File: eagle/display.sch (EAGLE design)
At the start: 6 parts

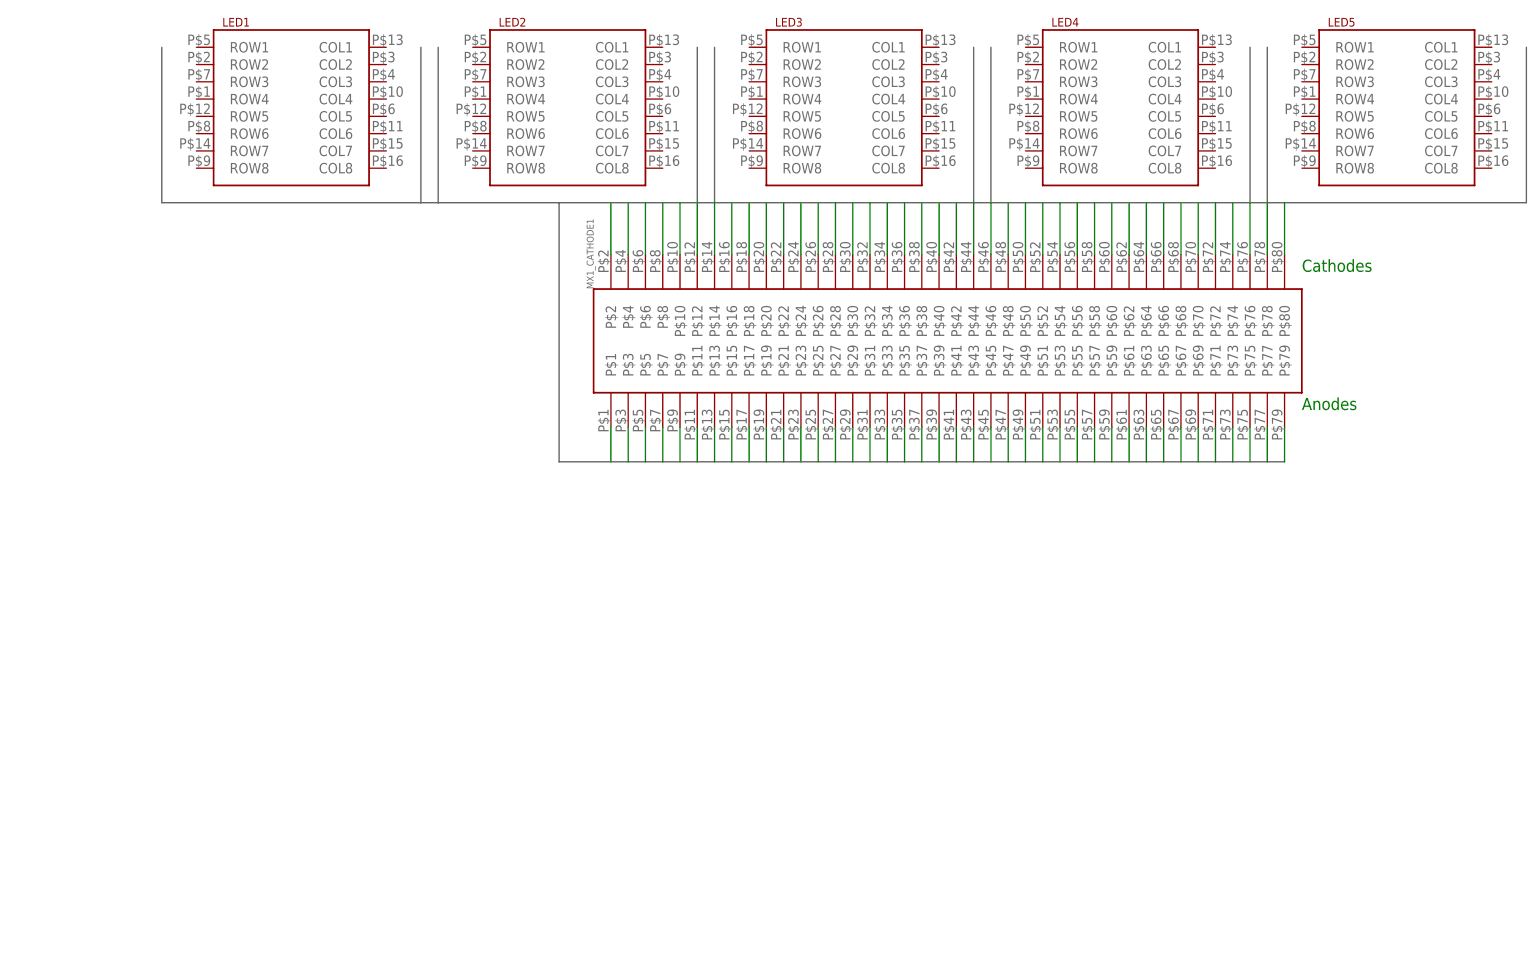
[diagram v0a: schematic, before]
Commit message: removed pinhead
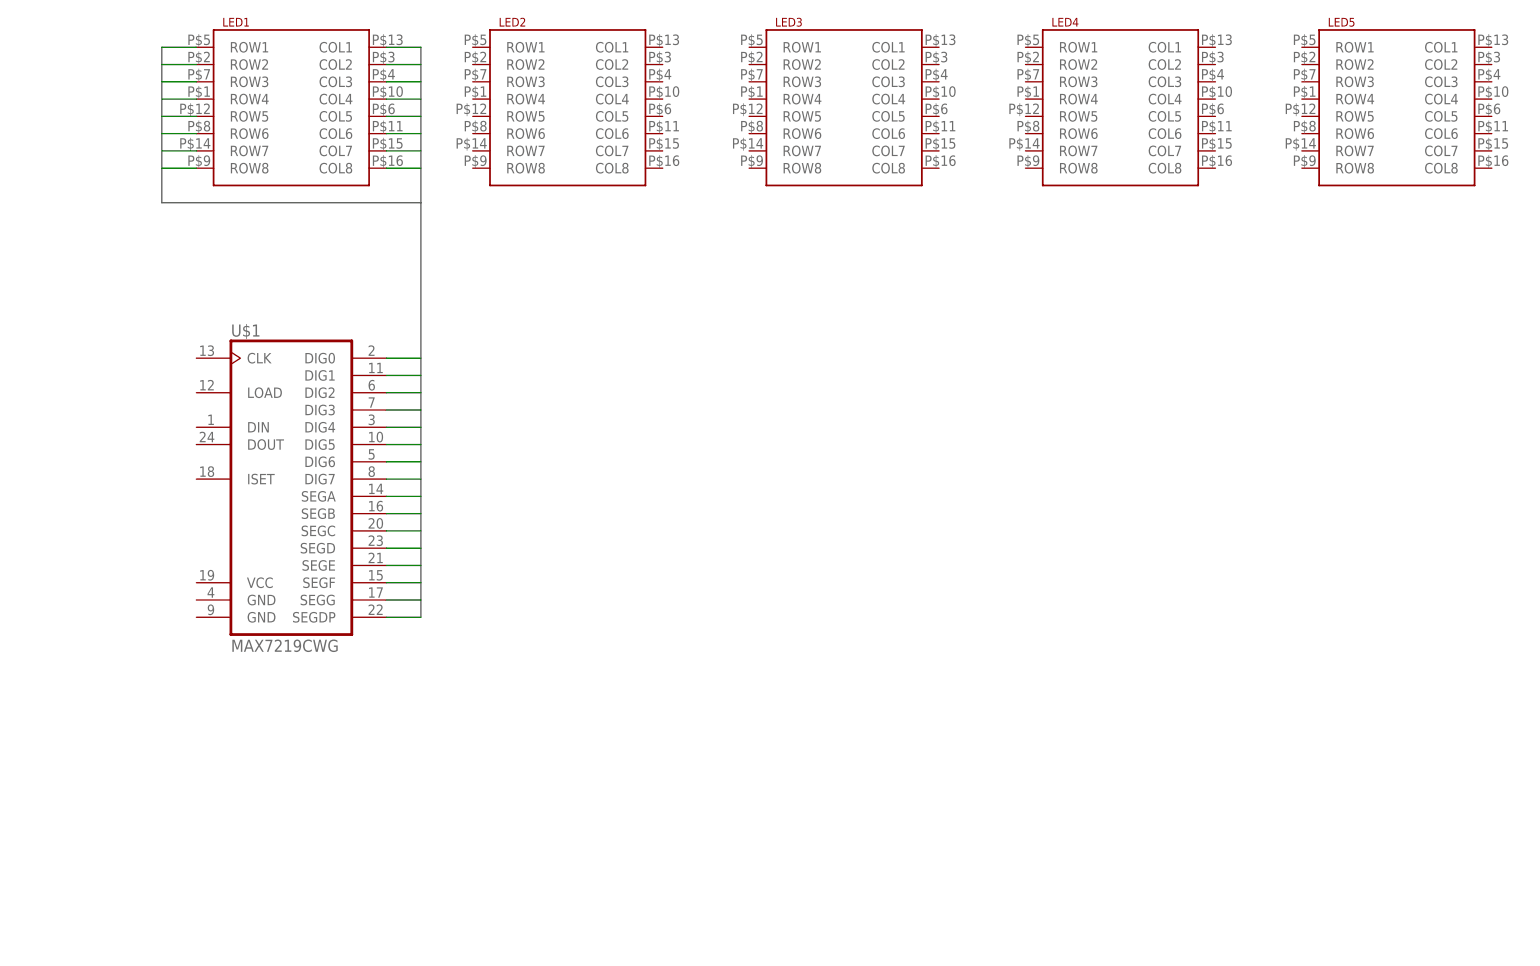
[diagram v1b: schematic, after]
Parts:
- removed U$6: PINHD-2X40FEMALE, pinhead-1.27:PINHD-2X40FEMALE
- added U$1: MAX7219CWG, max7219:MAX7219CWG
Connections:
- removed net MX1_ANODE1: U$6.P$1
- removed net MX1_ANODE2: U$6.P$3
- removed net MX1_ANODE3: U$6.P$5
- removed net MX1_ANODE4: U$6.P$7
- removed net MX1_ANODE5: U$6.P$9
- removed net MX1_ANODE6: U$6.P$11
- removed net MX1_ANODE7: U$6.P$13
- removed net MX1_ANODE8: U$6.P$15
- removed net MX1_CATHODE1: U$6.P$2
- removed net MX1_CATHODE2: U$6.P$4
- removed net MX1_CATHODE3: U$6.P$6
- removed net MX1_CATHODE4: U$6.P$8
- removed net MX1_CATHODE5: U$6.P$10
- removed net MX1_CATHODE6: U$6.P$12
- removed net MX1_CATHODE7: U$6.P$14
- removed net MX1_CATHODE8: U$6.P$16
- removed net MX2_ANODE1: U$6.P$17
- removed net MX2_ANODE2: U$6.P$19
- removed net MX2_ANODE3: U$6.P$21
- removed net MX2_ANODE4: U$6.P$23
- removed net MX2_ANODE5: U$6.P$25
- removed net MX2_ANODE6: U$6.P$27
- removed net MX2_ANODE7: U$6.P$29
- removed net MX2_ANODE8: U$6.P$31
- removed net MX2_CATHODE1: U$6.P$18
- removed net MX2_CATHODE2: U$6.P$20
- removed net MX2_CATHODE3: U$6.P$22
- removed net MX2_CATHODE4: U$6.P$24
- removed net MX2_CATHODE5: U$6.P$26
- removed net MX2_CATHODE6: U$6.P$28
- removed net MX2_CATHODE7: U$6.P$30
- removed net MX2_CATHODE8: U$6.P$32
- removed net MX3_ANODE1: U$6.P$33
- removed net MX3_ANODE2: U$6.P$35
- removed net MX3_ANODE3: U$6.P$37
- removed net MX3_ANODE4: U$6.P$39
- removed net MX3_ANODE5: U$6.P$41
- removed net MX3_ANODE6: U$6.P$43
- removed net MX3_ANODE7: U$6.P$45
- removed net MX3_ANODE8: U$6.P$47
- removed net MX3_CATHODE1: U$6.P$34
- removed net MX3_CATHODE2: U$6.P$36
- removed net MX3_CATHODE3: U$6.P$38
- removed net MX3_CATHODE4: U$6.P$40
- removed net MX3_CATHODE5: U$6.P$42
- removed net MX3_CATHODE6: U$6.P$44
- removed net MX3_CATHODE7: U$6.P$46
- removed net MX3_CATHODE8: U$6.P$48
- removed net MX4_ANODE1: U$6.P$49
- removed net MX4_ANODE2: U$6.P$51
- removed net MX4_ANODE3: U$6.P$53
- removed net MX4_ANODE4: U$6.P$55
- removed net MX4_ANODE5: U$6.P$57
- removed net MX4_ANODE6: U$6.P$59
- removed net MX4_ANODE7: U$6.P$61
- removed net MX4_ANODE8: U$6.P$63
- removed net MX4_CATHODE1: U$6.P$50
- removed net MX4_CATHODE2: U$6.P$52
- removed net MX4_CATHODE3: U$6.P$54
- removed net MX4_CATHODE4: U$6.P$56
- removed net MX4_CATHODE5: U$6.P$58
- removed net MX4_CATHODE6: U$6.P$60
- removed net MX4_CATHODE7: U$6.P$62
- removed net MX4_CATHODE8: U$6.P$64
- removed net MX5_ANODE1: U$6.P$65
- removed net MX5_ANODE2: U$6.P$67
- removed net MX5_ANODE3: U$6.P$69
- removed net MX5_ANODE4: U$6.P$71
- removed net MX5_ANODE5: U$6.P$73
- removed net MX5_ANODE6: U$6.P$75
- removed net MX5_ANODE7: U$6.P$77
- removed net MX5_ANODE8: U$6.P$79
- removed net MX5_CATHODE1: U$6.P$66
- removed net MX5_CATHODE2: U$6.P$68
- removed net MX5_CATHODE3: U$6.P$70
- removed net MX5_CATHODE4: U$6.P$72
- removed net MX5_CATHODE5: U$6.P$74
- removed net MX5_CATHODE6: U$6.P$76
- removed net MX5_CATHODE7: U$6.P$78
- removed net MX5_CATHODE8: U$6.P$80
- new net ANODE1: LED1.ROW1, U$1.SEGA
- new net ANODE2: LED1.ROW2, U$1.SEGB
- new net ANODE3: LED1.ROW3, U$1.SEGC
- new net ANODE4: LED1.ROW4, U$1.SEGD
- new net ANODE5: LED1.ROW5, U$1.SEGE
- new net ANODE6: LED1.ROW6, U$1.SEGF
- new net ANODE7: LED1.ROW7, U$1.SEGG
- new net ANODE8: LED1.ROW8, U$1.SEGDP
- new net CATHODE1: LED1.COL1, U$1.DIG0
- new net CATHODE2: LED1.COL2, U$1.DIG1
- new net CATHODE3: LED1.COL3, U$1.DIG2
- new net CATHODE4: LED1.COL4, U$1.DIG3
- new net CATHODE5: LED1.COL5, U$1.DIG4
- new net CATHODE6: LED1.COL6, U$1.DIG5
- new net CATHODE7: LED1.COL7, U$1.DIG6
- new net CATHODE8: LED1.COL8, U$1.DIG7
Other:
- note removed: "Anodes"
- note removed: "Cathodes"

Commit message: display board
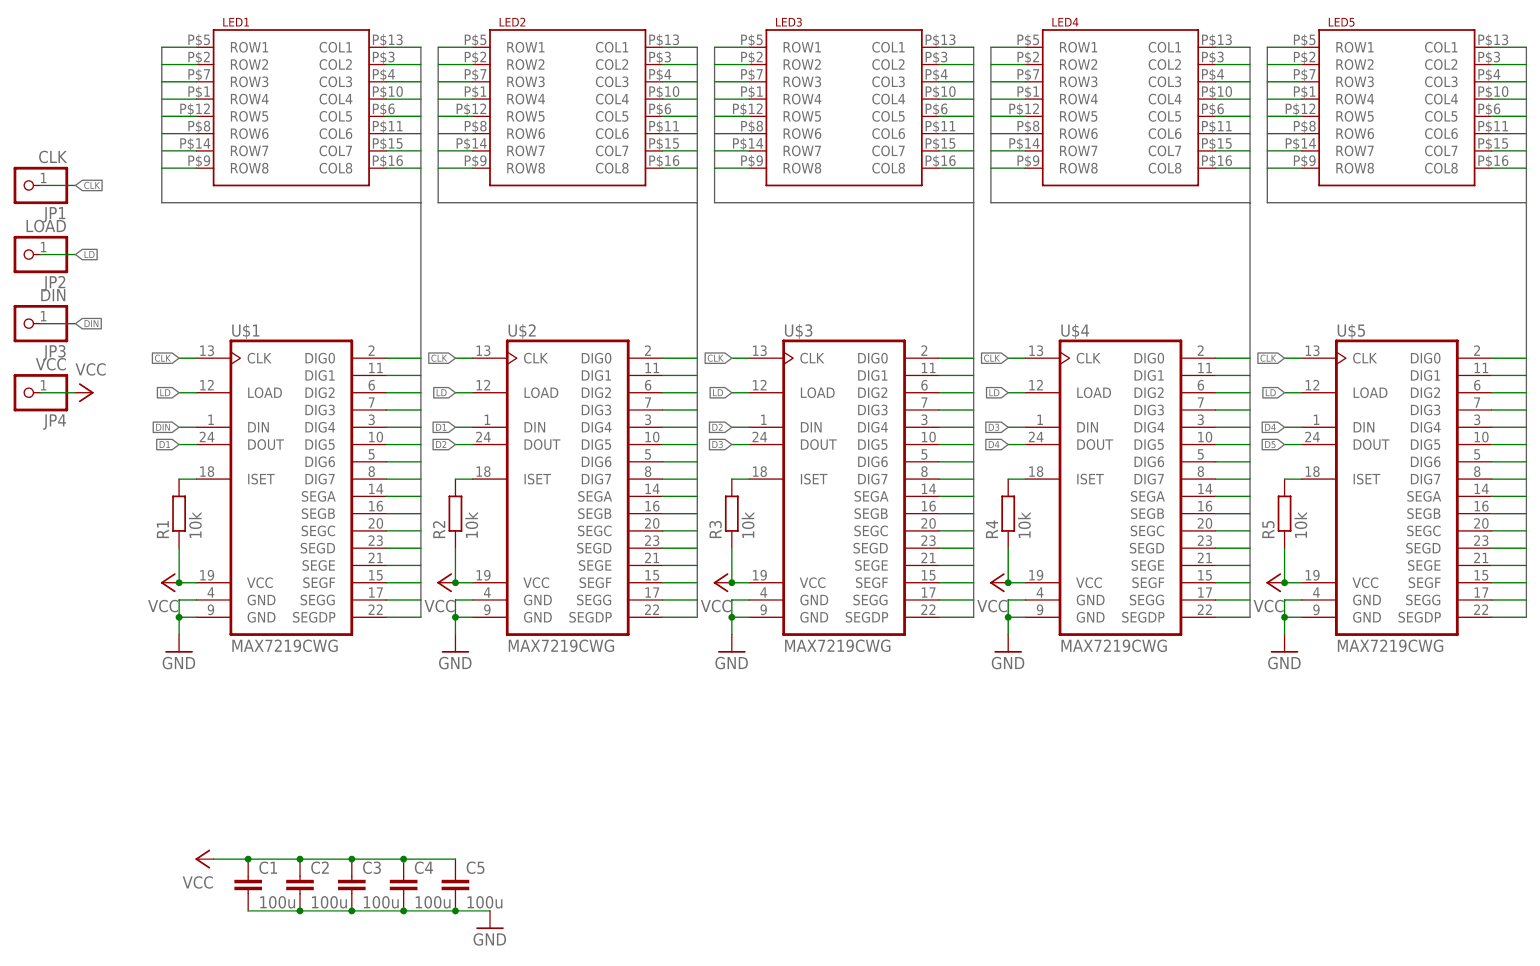
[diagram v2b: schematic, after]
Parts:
- added C1, C2, C3, C4, C5: 100u, rcl:C-EUC0805
- added JP1: CLK, pinhead:PINHD-1X1
- added JP2: LOAD, pinhead:PINHD-1X1
- added JP3: DIN, pinhead:PINHD-1X1
- added JP4: VCC, pinhead:PINHD-1X1
- added R1, R2, R3, R4, R5: 10k, rcl:R-EU_R0805
- added U$2, U$3, U$4, U$5: MAX7219CWG, max7219:MAX7219CWG
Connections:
- net ANODE1 renamed MATRIX1_ANODE1
- net ANODE2 renamed MATRIX1_ANODE2
- net ANODE3 renamed MATRIX1_ANODE3
- net ANODE4 renamed MATRIX1_ANODE4
- net ANODE5 renamed MATRIX1_ANODE5
- net ANODE6 renamed MATRIX1_ANODE6
- net ANODE7 renamed MATRIX1_ANODE7
- net ANODE8 renamed MATRIX1_ANODE8
- net CATHODE1 renamed MATRIX1_CATHODE1
- net CATHODE2 renamed MATRIX1_CATHODE2
- net CATHODE3 renamed MATRIX1_CATHODE3
- net CATHODE4 renamed MATRIX1_CATHODE4
- net CATHODE5 renamed MATRIX1_CATHODE5
- net CATHODE6 renamed MATRIX1_CATHODE6
- net CATHODE7 renamed MATRIX1_CATHODE7
- net CATHODE8 renamed MATRIX1_CATHODE8
- new net CLK: JP1.1, U$1.CLK, U$2.CLK, U$3.CLK, U$4.CLK, U$5.CLK
- new net D1: U$1.DOUT, U$2.DIN
- new net D2: U$2.DOUT, U$3.DIN
- new net D3: U$3.DOUT, U$4.DIN
- new net D4: U$4.DOUT, U$5.DIN
- new net D5: U$5.DOUT
- new net DIN: JP3.1, U$1.DIN
- new net GND: C1.2, C2.2, C3.2, C4.2, C5.2, U$1.GND@1, U$1.GND@2, U$2.GND@1, U$2.GND@2, U$3.GND@1, U$3.GND@2, U$4.GND@1, U$4.GND@2, U$5.GND@1, U$5.GND@2
- new net LD: JP2.1, U$1.LOAD, U$2.LOAD, U$3.LOAD, U$4.LOAD, U$5.LOAD
- new net MATRIX2_ANODE1: LED2.ROW1, U$2.SEGA
- new net MATRIX2_ANODE2: LED2.ROW2, U$2.SEGB
- new net MATRIX2_ANODE3: LED2.ROW3, U$2.SEGC
- new net MATRIX2_ANODE4: LED2.ROW4, U$2.SEGD
- new net MATRIX2_ANODE5: LED2.ROW5, U$2.SEGE
- new net MATRIX2_ANODE6: LED2.ROW6, U$2.SEGF
- new net MATRIX2_ANODE7: LED2.ROW7, U$2.SEGG
- new net MATRIX2_ANODE8: LED2.ROW8, U$2.SEGDP
- new net MATRIX2_CATHODE1: LED2.COL1, U$2.DIG0
- new net MATRIX2_CATHODE2: LED2.COL2, U$2.DIG1
- new net MATRIX2_CATHODE3: LED2.COL3, U$2.DIG2
- new net MATRIX2_CATHODE4: LED2.COL4, U$2.DIG3
- new net MATRIX2_CATHODE5: LED2.COL5, U$2.DIG4
- new net MATRIX2_CATHODE6: LED2.COL6, U$2.DIG5
- new net MATRIX2_CATHODE7: LED2.COL7, U$2.DIG6
- new net MATRIX2_CATHODE8: LED2.COL8, U$2.DIG7
- new net MATRIX3_ANODE1: LED3.ROW1, U$3.SEGA
- new net MATRIX3_ANODE2: LED3.ROW2, U$3.SEGB
- new net MATRIX3_ANODE3: LED3.ROW3, U$3.SEGC
- new net MATRIX3_ANODE4: LED3.ROW4, U$3.SEGD
- new net MATRIX3_ANODE5: LED3.ROW5, U$3.SEGE
- new net MATRIX3_ANODE6: LED3.ROW6, U$3.SEGF
- new net MATRIX3_ANODE7: LED3.ROW7, U$3.SEGG
- new net MATRIX3_ANODE8: LED3.ROW8, U$3.SEGDP
- new net MATRIX3_CATHODE1: LED3.COL1, U$3.DIG0
- new net MATRIX3_CATHODE2: LED3.COL2, U$3.DIG1
- new net MATRIX3_CATHODE3: LED3.COL3, U$3.DIG2
- new net MATRIX3_CATHODE4: LED3.COL4, U$3.DIG3
- new net MATRIX3_CATHODE5: LED3.COL5, U$3.DIG4
- new net MATRIX3_CATHODE6: LED3.COL6, U$3.DIG5
- new net MATRIX3_CATHODE7: LED3.COL7, U$3.DIG6
- new net MATRIX3_CATHODE8: LED3.COL8, U$3.DIG7
- new net MATRIX4_ANODE1: LED4.ROW1, U$4.SEGA
- new net MATRIX4_ANODE2: LED4.ROW2, U$4.SEGB
- new net MATRIX4_ANODE3: LED4.ROW3, U$4.SEGC
- new net MATRIX4_ANODE4: LED4.ROW4, U$4.SEGD
- new net MATRIX4_ANODE5: LED4.ROW5, U$4.SEGE
- new net MATRIX4_ANODE6: LED4.ROW6, U$4.SEGF
- new net MATRIX4_ANODE7: LED4.ROW7, U$4.SEGG
- new net MATRIX4_ANODE8: LED4.ROW8, U$4.SEGDP
- new net MATRIX4_CATHODE1: LED4.COL1, U$4.DIG0
- new net MATRIX4_CATHODE2: LED4.COL2, U$4.DIG1
- new net MATRIX4_CATHODE3: LED4.COL3, U$4.DIG2
- new net MATRIX4_CATHODE4: LED4.COL4, U$4.DIG3
- new net MATRIX4_CATHODE5: LED4.COL5, U$4.DIG4
- new net MATRIX4_CATHODE6: LED4.COL6, U$4.DIG5
- new net MATRIX4_CATHODE7: LED4.COL7, U$4.DIG6
- new net MATRIX4_CATHODE8: LED4.COL8, U$4.DIG7
- new net MATRIX5_ANODE1: LED5.ROW1, U$5.SEGA
- new net MATRIX5_ANODE2: LED5.ROW2, U$5.SEGB
- new net MATRIX5_ANODE3: LED5.ROW3, U$5.SEGC
- new net MATRIX5_ANODE4: LED5.ROW4, U$5.SEGD
- new net MATRIX5_ANODE5: LED5.ROW5, U$5.SEGE
- new net MATRIX5_ANODE6: LED5.ROW6, U$5.SEGF
- new net MATRIX5_ANODE7: LED5.ROW7, U$5.SEGG
- new net MATRIX5_ANODE8: LED5.ROW8, U$5.SEGDP
- new net MATRIX5_CATHODE1: LED5.COL1, U$5.DIG0
- new net MATRIX5_CATHODE2: LED5.COL2, U$5.DIG1
- new net MATRIX5_CATHODE3: LED5.COL3, U$5.DIG2
- new net MATRIX5_CATHODE4: LED5.COL4, U$5.DIG3
- new net MATRIX5_CATHODE5: LED5.COL5, U$5.DIG4
- new net MATRIX5_CATHODE6: LED5.COL6, U$5.DIG5
- new net MATRIX5_CATHODE7: LED5.COL7, U$5.DIG6
- new net MATRIX5_CATHODE8: LED5.COL8, U$5.DIG7
- new net N$1: R5.2, U$5.ISET
- new net N$10: R2.2, U$2.ISET
- new net N$15: R3.2, U$3.ISET
- new net N$20: R4.2, U$4.ISET
- new net N$5: R1.2, U$1.ISET
- new net VCC: C1.1, C2.1, C3.1, C4.1, C5.1, JP4.1, R1.1, R2.1, R3.1, R4.1, R5.1, U$1.VCC, U$2.VCC, U$3.VCC, U$4.VCC, U$5.VCC
